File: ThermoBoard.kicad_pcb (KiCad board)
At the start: 4 copper layers, 97 x 97 mm, 139 parts, among them J100 Conn_01x05_Pin, J101 Screw_Terminal_01x02, J102 USB_C_Receptacle_USB2.0_16P, J200 RJ45_Hanrun_HR911105A_Horizon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, J300 PCC-SMP-K-5, J301 PCC-SMP-K-5, J302 PCC-SMP-K-5, J303 PCC-SMP-K-5, J400 Conn_01x03, Q100 Si2371EDS, SW100 SKRPANE010, U100 STM32H563RITx, U101 AP2112K-3.3, U102 USBLC6-2SC6, U200 LAN8742A, U300 MAX31856, U301 MAX31856, U302 MAX31856, U303 MAX31856, U400 TJA1042T-3, Y100 16MHz, Y200 25MHz

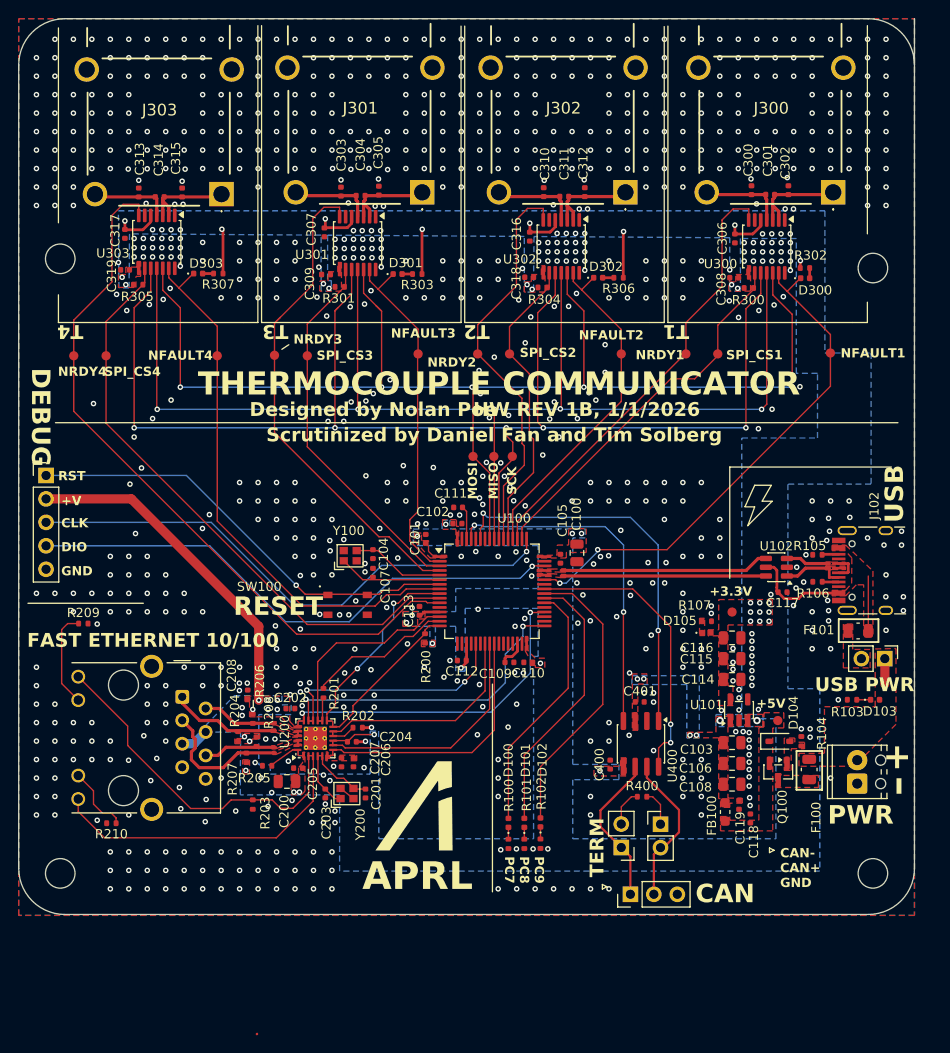
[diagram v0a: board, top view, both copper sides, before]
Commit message: fix DRC Problems
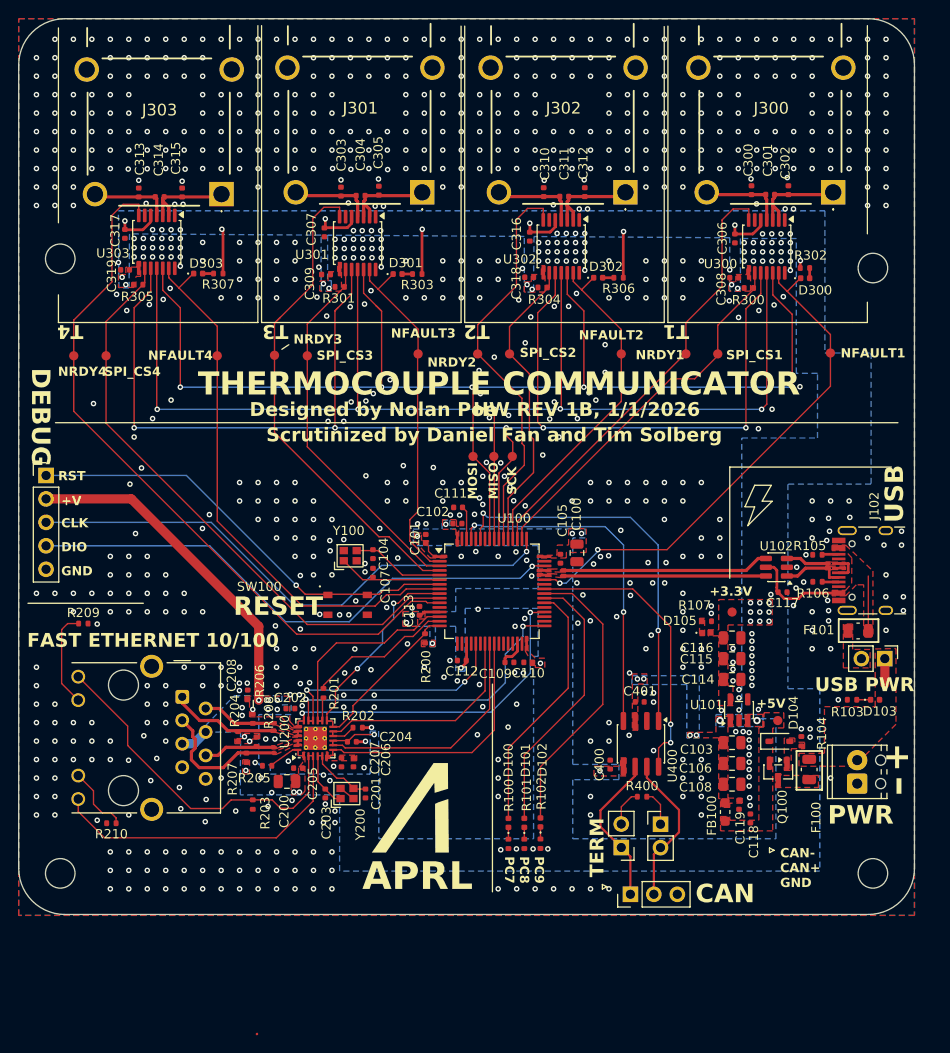
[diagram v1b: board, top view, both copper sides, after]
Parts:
- removed #SYM200: APRL_Logo_2Layer-v1, Library:APRL_Logo_2Layer-v1
- added REF**: APRL_Logo_2Layer-v1, Library:APRL_Logo_2Layer-v1-noct, F.Cu at (134.5, 142.9)
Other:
- outline, holes or cut-outs redrawn
